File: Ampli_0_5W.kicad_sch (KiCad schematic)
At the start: 69 parts, among them J1002 RF_In, J1003 PTT_In, J1005 Aux_PTT_Out, J1006 RF_Out, Q1001 2N7002, Q1002 FDD6685, Q1005 2N5109, Q1006 AFT05MP075N, T1001 4:1, T1002 1:1, T1003 1:9, U1001 L78L05_SO8

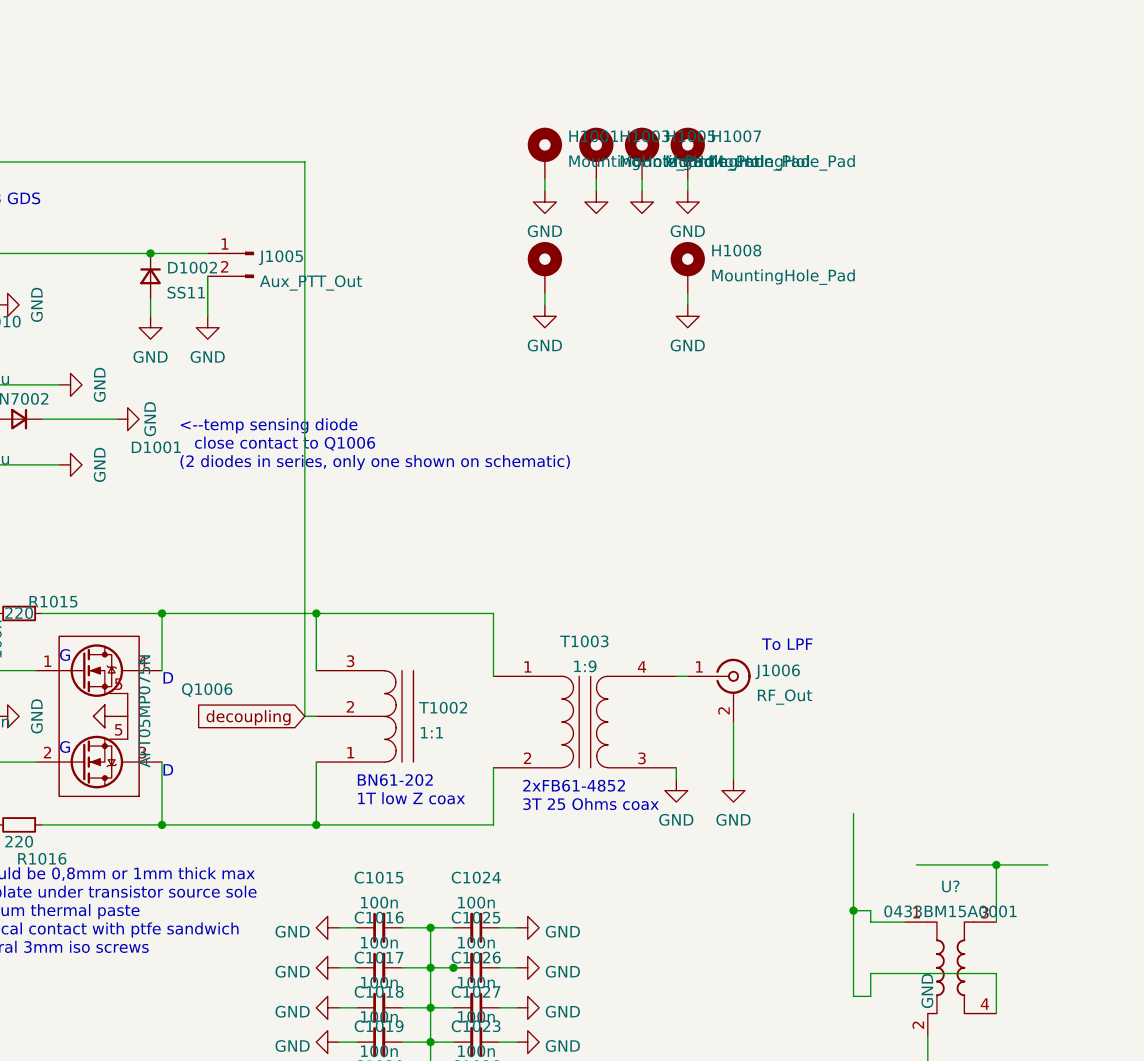
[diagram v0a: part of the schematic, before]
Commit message: release 2.0, shorter drain path
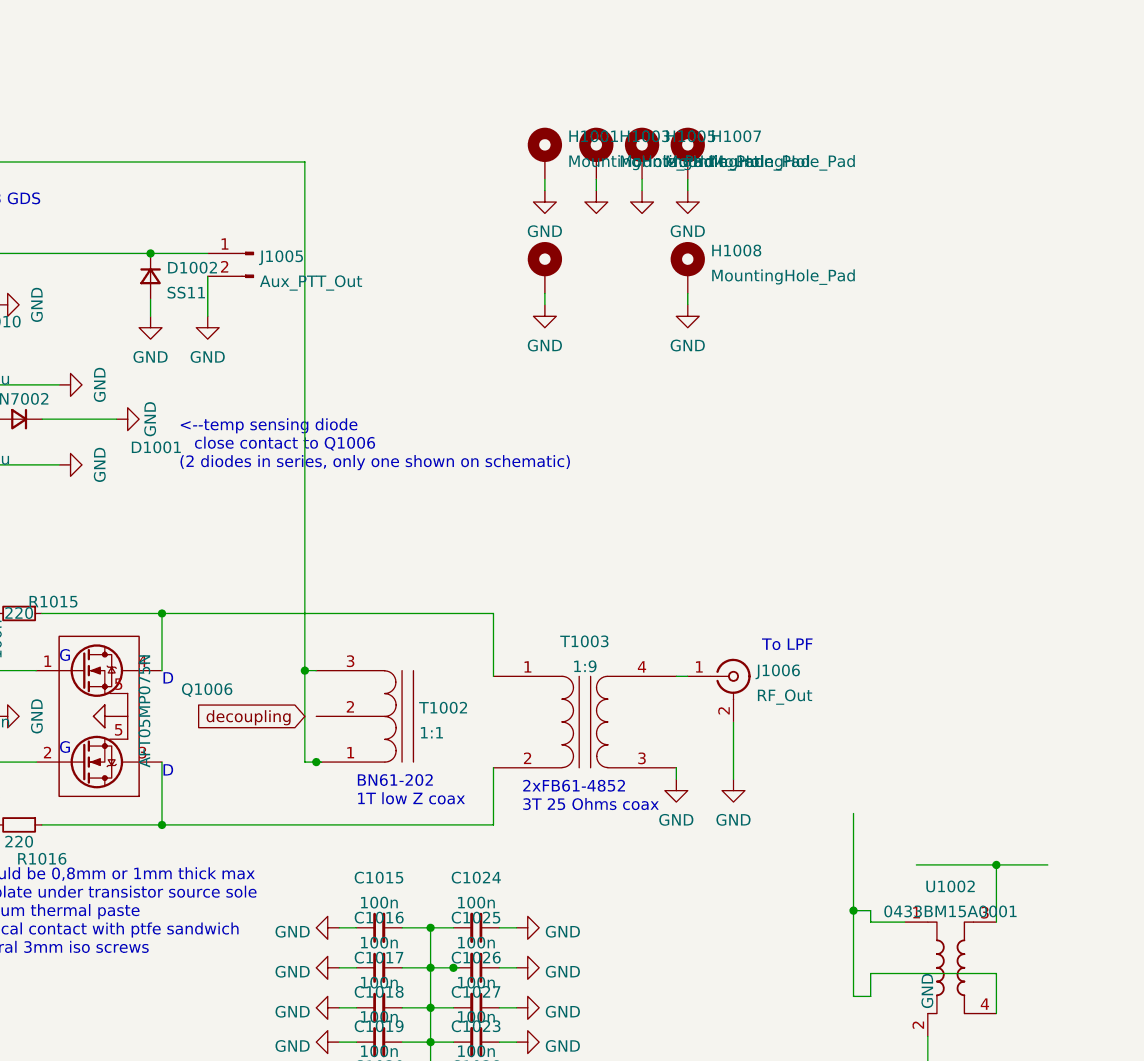
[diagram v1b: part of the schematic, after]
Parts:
- C1013, C1014: footprint Capacitor_SMD:C_0805_2012Metric_Pad1.18x1.45mm_HandSolder -> Capacitor_SMD:C_1206_3216Metric_Pad1.33x1.80mm_HandSolder
- C1015, C1016, C1017, C1018, C1019, C1020, C1021, C1022, C1023, C1024, C1025, C1026, C1027, C1028, C1029, C1030: footprint Capacitor_SMD:C_0805_2012Metric_Pad1.18x1.45mm_HandSolder -> Capacitor_SMD:C_1210_3225Metric_Pad1.33x2.70mm_HandSolder
- gave numbers to parts that had none: 1
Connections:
- net +12V: now also T1002.1 (SA), T1002.3 (SC); no longer T1002.2 (SB)
- net at Q1006.3 (D), R1016.1, T1003.2 (AB): no longer T1002.1 (SA)
- net at Q1006.4 (D), R1015.1, T1003.1 (AA): no longer T1002.3 (SC)

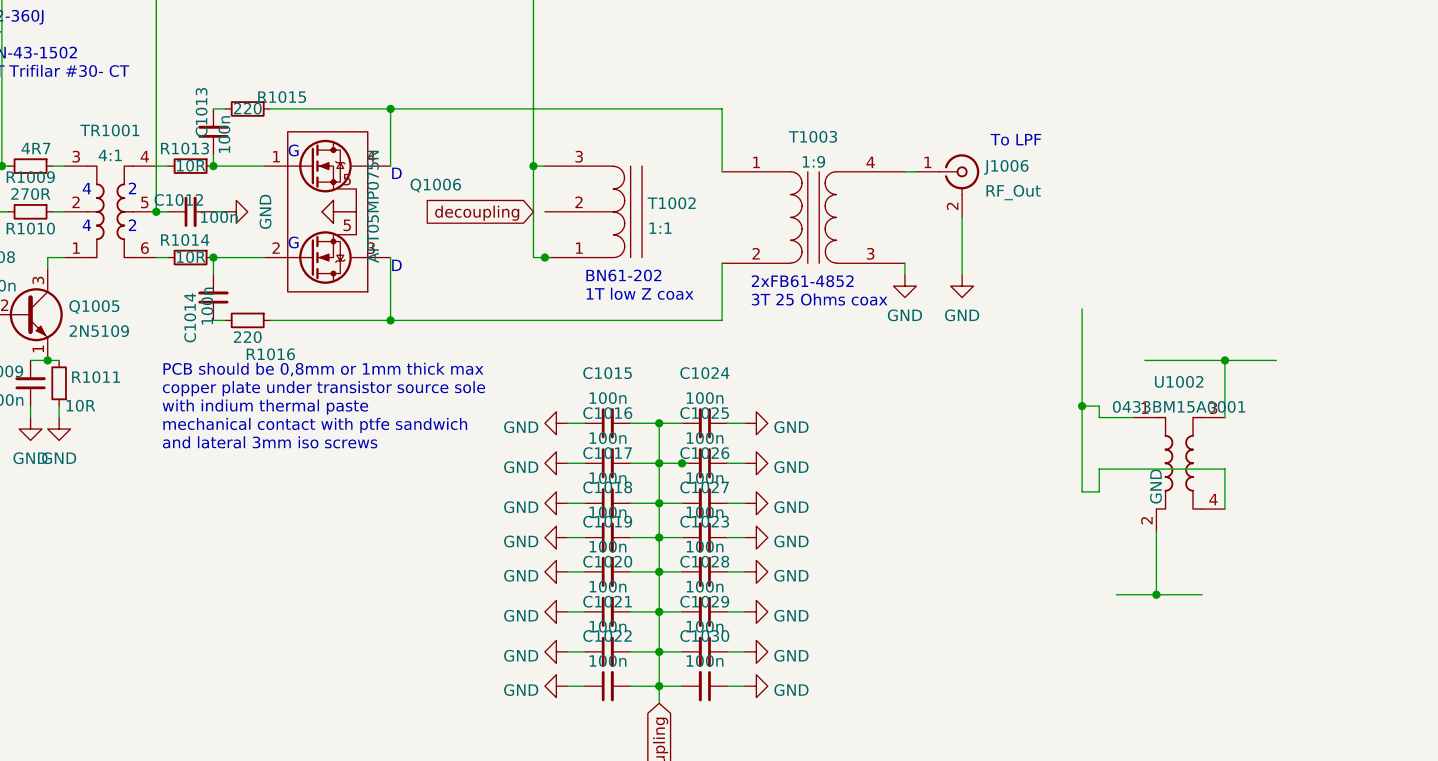
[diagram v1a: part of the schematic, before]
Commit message: shorten drain circuit, new gerber, new ibom
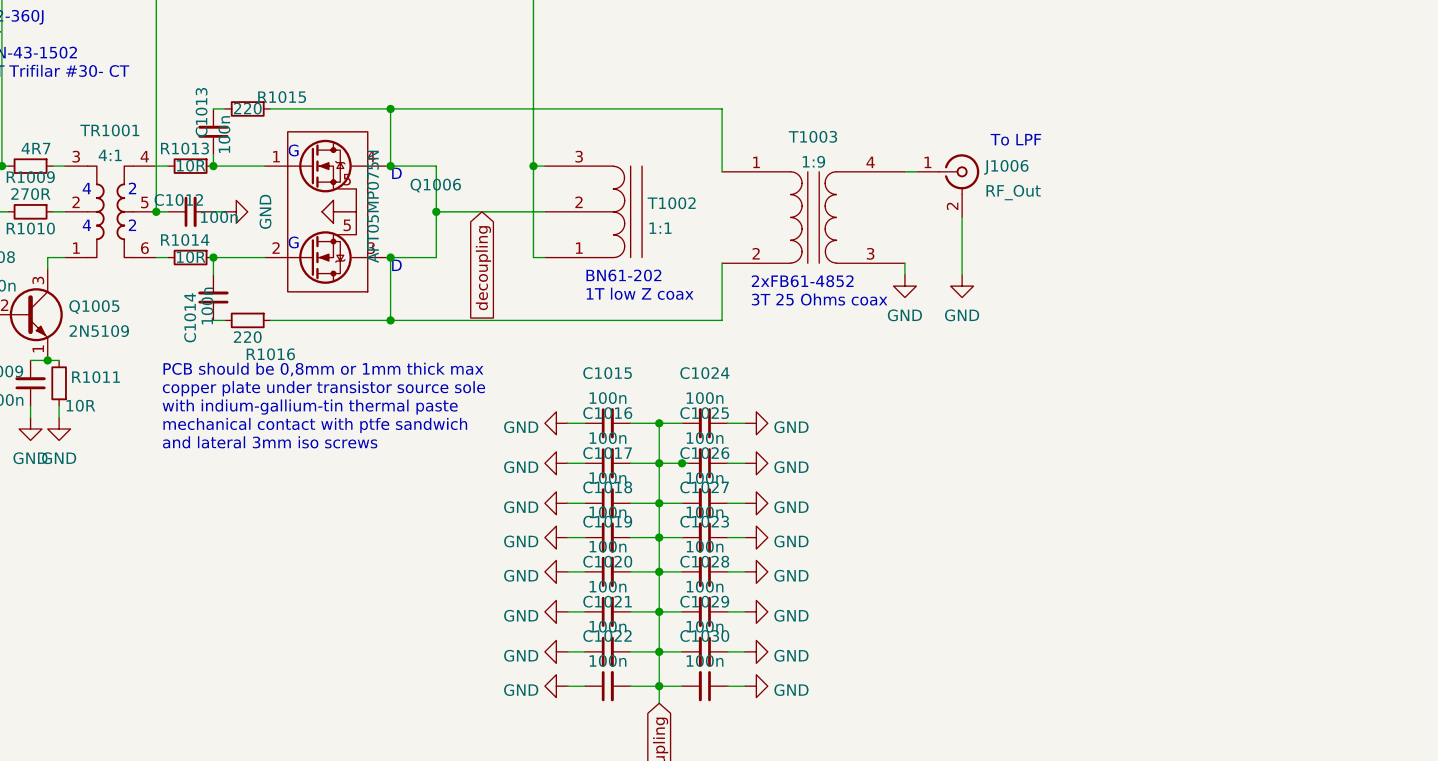
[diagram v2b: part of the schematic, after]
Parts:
- removed U1002: 0433BM15A0001, RF_Converter:Balun_Johanson_0896BM15A0001, symbol Transformer:0433BM15A0001
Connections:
- net +12V: no longer C1015.2, C1016.2, C1017.2, C1018.2, C1019.2, C1020.2, C1021.2, C1022.2, C1023.2, C1024.2, C1025.2, C1026.2, C1027.2, C1028.2, C1029.2, C1030.2
- net decoupling: now reaches Q1006.3 (D), R1016.1, T1003.2 (AB)
- net decoupling: now also C1015.2, C1016.2, C1017.2, C1018.2, C1019.2, C1020.2, C1021.2, C1022.2, C1023.2, C1024.2, C1025.2, C1026.2, C1027.2, C1028.2, C1029.2, C1030.2, Q1006.4 (D), R1015.1, T1002.2 (SB), T1003.1 (AA)
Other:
- note added: "PCB should be 0,8mm or 1mm thick max copper plate under transistor source sole with indium-gallium-tin thermal paste mechanical contact with ptfe sandwich and lateral 3mm iso screws"
- note removed: "PCB should be 0,8mm or 1mm thick max copper plate under transistor source sole with indium thermal paste mechanical contact with ptfe sandwich and lateral 3mm iso screws"
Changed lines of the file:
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@@
   (junction (at 146.05 151.13) (diameter 0) (color 0 0 0 0)
   )
-  (junction (at 201.295 140.97) (diameter 0) (color 0 0 0 0)
+  (junction (at 121.285 98.425) (diameter 0) (color 0 0 0 0)
   )
   (junction (at 43.815 36.83) (diameter 0) (color 0 0 0 0)
@@
   (junction (at 90.17 70.485) (diameter 0) (color 0 0 0 0)
   )
-  (junction (at 208.915 114.935) (diameter 0) (color 0 0 0 0)
-  )
   (junction (at 146.05 138.43) (diameter 0) (color 0 0 0 0)
   )
@@
   (junction (at 50.165 54.61) (diameter 0) (color 0 0 0 0)
   )
-  (junction (at 133.35 103.505) (diameter 0) (color 0 0 0 0)
-  )
   (junction (at 59.055 36.83) (diameter 0) (color 0 0 0 0)
   )
@@
   (junction (at 146.05 121.92) (diameter 0) (color 0 0 0 0)
   )
+  (junction (at 116.205 103.505) (diameter 0) (color 0 0 0 0)
+  )
   (junction (at 116.205 110.49) (diameter 0) (color 0 0 0 0)
   )
-  (junction (at 193.04 120.015) (diameter 0) (color 0 0 0 0)
-  )
   (junction (at 146.05 142.875) (diameter 0) (color 0 0 0 0)
   )
@@
   (junction (at 70.485 98.425) (diameter 0) (color 0 0 0 0)
   )
+  (junction (at 116.205 93.345) (diameter 0) (color 0 0 0 0)
+  )
   (junction (at 116.205 86.995) (diameter 0) (color 0 0 0 0)
   )
@@
     (stroke (width 0) (type default) (color 0 0 0 0))
   )
-  (wire (pts (xy 196.85 140.97) (xy 201.295 140.97))
-    (stroke (width 0) (type default) (color 0 0 0 0))
-  )
   (wire (pts (xy 116.205 103.505) (xy 116.205 110.49))
     (stroke (width 0) (type default) (color 0 0 0 0))
@@
     (stroke (width 0) (type default) (color 0 0 0 0))
   )
-  (wire (pts (xy 193.04 109.22) (xy 193.04 120.015))
-    (stroke (width 0) (type default) (color 0 0 0 0))
-  )
   (wire (pts (xy 132.08 93.345) (xy 133.35 93.345))
     (stroke (width 0) (type default) (color 0 0 0 0))
@@
     (stroke (width 0) (type default) (color 0 0 0 0))
   )
-  (wire (pts (xy 133.35 103.505) (xy 132.08 103.505))
-    (stroke (width 0) (type default) (color 0 0 0 0))
-  )
   (wire (pts (xy 142.875 130.81) (xy 146.05 130.81))
     (stroke (width 0) (type default) (color 0 0 0 0))
@@
     (stroke (width 0) (type default) (color 0 0 0 0))
   )
-  (wire (pts (xy 193.04 120.015) (xy 193.04 129.54))
-    (stroke (width 0) (type default) (color 0 0 0 0))
-  )
   (wire (pts (xy 63.5 41.91) (xy 65.405 41.91))
     (stroke (width 0) (type default) (color 0 0 0 0))
@@
     (stroke (width 0) (type default) (color 0 0 0 0))
   )
-  (wire (pts (xy 208.915 131.445) (xy 208.915 127))
-    (stroke (width 0) (type default) (color 0 0 0 0))
-  )
   (wire (pts (xy 65.405 108.585) (xy 65.405 109.855))
     (stroke (width 0) (type default) (color 0 0 0 0))
@@
     (stroke (width 0) (type default) (color 0 0 0 0))
   )
+  (wire (pts (xy 121.285 98.425) (xy 121.285 93.345))
+    (stroke (width 0) (type default) (color 0 0 0 0))
+  )
+  (wire (pts (xy 121.285 98.425) (xy 121.285 103.505))
+    (stroke (width 0) (type default) (color 0 0 0 0))
+  )
   (wire (pts (xy 96.52 98.425) (xy 97.79 98.425))
     (stroke (width 0) (type default) (color 0 0 0 0))
@@
     (stroke (width 0) (type default) (color 0 0 0 0))
   )
-  (wire (pts (xy 208.915 127) (xy 194.945 127))
-    (stroke (width 0) (type default) (color 0 0 0 0))
-  )
-  (wire (pts (xy 198.755 121.285) (xy 194.945 121.285))
-    (stroke (width 0) (type default) (color 0 0 0 0))
-  )
   (wire (pts (xy 50.165 54.61) (xy 51.435 54.61))
     (stroke (width 0) (type default) (color 0 0 0 0))
@@
     (stroke (width 0) (type default) (color 0 0 0 0))
   )
-  (wire (pts (xy 208.915 114.935) (xy 214.63 114.935))
-    (stroke (width 0) (type default) (color 0 0 0 0))
-  )
   (wire (pts (xy 146.05 142.875) (xy 146.05 138.43))
     (stroke (width 0) (type default) (color 0 0 0 0))
@@
     (stroke (width 0) (type default) (color 0 0 0 0))
   )
-  (wire (pts (xy 193.04 120.015) (xy 194.945 120.015))
-    (stroke (width 0) (type default) (color 0 0 0 0))
-  )
   (wire (pts (xy 78.105 114.935) (xy 79.375 114.935))
     (stroke (width 0) (type default) (color 0 0 0 0))
   )
+  (wire (pts (xy 132.08 103.505) (xy 133.35 103.505))
+    (stroke (width 0) (type default) (color 0 0 0 0))
+  )
   (wire (pts (xy 52.705 99.06) (xy 52.705 104.775))
     (stroke (width 0) (type default) (color 0 0 0 0))
@@
     (stroke (width 0) (type default) (color 0 0 0 0))
   )
-  (wire (pts (xy 201.295 140.97) (xy 206.375 140.97))
-    (stroke (width 0) (type default) (color 0 0 0 0))
-  )
-  (wire (pts (xy 200.025 114.935) (xy 208.915 114.935))
-    (stroke (width 0) (type default) (color 0 0 0 0))
-  )
   (wire (pts (xy 121.285 49.53) (xy 121.285 53.975))
     (stroke (width 0) (type default) (color 0 0 0 0))
@@
     (stroke (width 0) (type default) (color 0 0 0 0))
   )
-  (wire (pts (xy 208.915 121.285) (xy 208.915 114.935))
-    (stroke (width 0) (type default) (color 0 0 0 0))
-  )
   (wire (pts (xy 137.795 130.81) (xy 135.89 130.81))
     (stroke (width 0) (type default) (color 0 0 0 0))
@@
     (stroke (width 0) (type default) (color 0 0 0 0))
   )
-  (wire (pts (xy 194.945 127) (xy 194.945 129.54))
-    (stroke (width 0) (type default) (color 0 0 0 0))
-  )
   (wire (pts (xy 90.17 52.705) (xy 91.44 52.705))
     (stroke (width 0) (type default) (color 0 0 0 0))
@@
     (stroke (width 0) (type default) (color 0 0 0 0))
   )
-  (wire (pts (xy 201.295 133.985) (xy 201.295 140.97))
-    (stroke (width 0) (type default) (color 0 0 0 0))
-  )
   (wire (pts (xy 137.795 134.62) (xy 135.89 134.62))
     (stroke (width 0) (type default) (color 0 0 0 0))
@@
     (stroke (width 0) (type default) (color 0 0 0 0))
   )
-  (wire (pts (xy 194.945 120.015) (xy 194.945 121.285))
+  (wire (pts (xy 133.35 98.425) (xy 121.285 98.425))
     (stroke (width 0) (type default) (color 0 0 0 0))
   )
@@
     (stroke (width 0) (type default) (color 0 0 0 0))
   )
-  (wire (pts (xy 194.945 129.54) (xy 193.04 129.54))
+  (wire (pts (xy 121.285 103.505) (xy 116.205 103.505))
     (stroke (width 0) (type default) (color 0 0 0 0))
   )
@@
     (stroke (width 0) (type default) (color 0 0 0 0))
   )
+  (wire (pts (xy 116.205 93.345) (xy 121.285 93.345))
+    (stroke (width 0) (type default) (color 0 0 0 0))
+  )
   (wire (pts (xy 90.17 61.595) (xy 91.44 61.595))
     (stroke (width 0) (type default) (color 0 0 0 0))
@@
   )
   (wire (pts (xy 153.67 130.81) (xy 155.575 130.81))
-    (stroke (width 0) (type default) (color 0 0 0 0))
-  )
-  (wire (pts (xy 133.985 103.505) (xy 133.35 103.505))
     (stroke (width 0) (type default) (color 0 0 0 0))
   )
@@
     (effects (font (size 1.27 1.27)) (justify left bottom))
   )
-  (text "PCB should be 0,8mm or 1mm thick max\ncopper plate under transistor source sole \nwith indium thermal paste\nmechanical contact with ptfe sandwich\nand lateral 3mm iso screws"
+  (text "PCB should be 0,8mm or 1mm thick max\ncopper plate under transistor source sole \nwith indium-gallium-tin thermal paste\nmechanical contact with ptfe sandwich\nand lateral 3mm iso screws"
     (at 90.805 125.095 0)
     (effects (font (size 1.27 1.27)) (justify left bottom))
@@
     )
   )
-  (global_label "decoupling" (shape input) (at 132.08 98.425 180) (fields_autoplaced)
+  (global_label "decoupling" (shape input) (at 126.365 98.425 270) (fields_autoplaced)
     (effects (font (size 1.27 1.27)) (justify right))
-    (property "Intersheet References" "${INTERSHEET_REFS}" (id 0) (at 119.3255 98.3456 0)
+    (property "Intersheet References" "${INTERSHEET_REFS}" (id 0) (at 126.2856 111.1795 90)
       (effects (font (size 1.27 1.27)) (justify right) hide)
     )
@@
     (pin "2")
     (pin "3")
-  )
-  (symbol (lib_id "Transformer:0433BM15A0001") (at 203.835 126.365 0) (unit 1)
-    (in_bom yes) (on_board yes) (fields_autoplaced)
-    (property "Reference" "U1002" (id 0) (at 203.835 117.3693 0))
-    (property "Value" "0433BM15A0001" (id 1) (at 203.835 120.1444 0))
-    (property "Footprint" "RF_Converter:Balun_Johanson_0896BM15A0001" (id 2) (at 203.835 133.985 0)
-      (effects (font (size 1.27 1.27)) hide)
-    )
-    (property "Datasheet" "https://www.johansontechnology.com/datasheets/0433BM15A0001/0433BM15A0001.pdf" (id 3) (at 203.835 118.745 0)
-      (effects (font (size 1.27 1.27)) hide)
-    )
-    (pin "1")
-    (pin "2")
-    (pin "3")
-    (pin "4")
-    (pin "5")
-    (pin "6")
   )
   (symbol (lib_id "power:GND") (at 155.575 126.365 90) (unit 1)
@@
       (reference "U1001") (unit 1) (value "L78L05_SO8") (footprint "Package_SO:SOIC-8_3.9x4.9mm_P1.27mm")
     )
-    (path "/44d77947-e58b-4905-bc5c-c957fb08ea72"
-      (reference "U1002") (unit 1) (value "0433BM15A0001") (footprint "RF_Converter:Balun_Johanson_0896BM15A0001")
-    )
-  )
+  )

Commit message: Diomedes V1.0 final with correct psu, bias & drain trace
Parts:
- removed H1001, H1003: MountingHole_Pad, MountingHole:MountingHole_3.2mm_M3_DIN965_Pad, symbol Mechanical:MountingHole_Pad
- removed U1001: L78L05_SO8, Package_SO:SOIC-8_3.9x4.9mm_P1.27mm, symbol Regulator_Linear:L78L05_SO8
- added U1: LM78M05_TO252, Package_TO_SOT_SMD:TO-252-2, symbol Regulator_Linear:LM78M05_TO252
- renumbered C1003 to C1, C1001 to C10, C1012 to C11, C1013 to C12, C1014 to C13, C1015 to C14, C1016 to C15, C1017 to C16, C1018 to C17, C1019 to C18, C1020 to C19, C1004 to C2, C1021 to C20, C1022 to C21, C1024 to C22, C1025 to C23, C1026 to C24, C1027 to C25, C1023 to C26, C1028 to C27, C1029 to C28, C1030 to C29, C1005 to C3, C1006 to C4, C1007 to C5, C1008 to C6, C1009 to C7, C1010 to C8, C1011 to C9, D1001 to D1, D1002 to D2, H1006 to H1, H1004 to H2, H1002 to H4, H1005 to H6, H1007 to H7, H1008 to H8, J1002 to J1, J1003 to J2, J1005 to J3, J1006 to J4, Q1001 to Q1, Q1002 to Q2, Q1005 to Q3, Q1006 to Q4, R1002 to R1, R1011 to R10, R1012 to R11, R1013 to R12, R1014 to R13, R1015 to R14, R1016 to R15, R1003 to R2, R1004 to R3, R1005 to R4, R1006 to R5, R1007 to R6, R1008 to R7, R1009 to R8, R1010 to R9, RV1001 to RV1, T1001 to T1, T1002 to T2, T1003 to T3, TR1001 to TR1
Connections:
- net +12V: now also C14.2, C15.2, C16.2, C17.2, C18.2, C19.2, C20.2, C21.2, C22.2, C23.2, C24.2, C25.2, C26.2, C27.2, C28.2, C29.2, Q2.3 (S); no longer Q2.2 (D)
- net GND: now also U1.2 (GND)
- net at C8.1, RV1.1, RV1.2: now also U1.3 (VO)
- net at C5.1, D2.1 (K), J3.1 (Pin_1)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: now also Q2.2 (D), U1.1 (VI); no longer Q2.3 (S)
- removed net decoupling: C14.2, C15.2, C16.2, C17.2, C18.2, C19.2, C20.2, C21.2, C22.2, C23.2, C24.2, C25.2, C26.2, C27.2, C28.2, C29.2, Q4.3 (D), Q4.4 (D), R14.1, R15.1, T2.2 (SB), T3.1 (AA), T3.2 (AB)
- new net: Q4.3 (D), Q4.4 (D), R14.1, R15.1, T2.2 (SB), T3.1 (AA), T3.2 (AB)
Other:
- note added: "Ajouter une entrée tx to gnd (gate de Q1002)"
- note added: "From Red Pitaya - TX/RX E1-3 - Gnd E1 25/26 Active = high"
- note added: "Todo - Vérifier perçages de fixation - Vérifier contact semelle/pcb/gnd (plaquage transistor)"
- moved on the sheet: H6

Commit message: Diomedes V2.0 final, bias OK
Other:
- note added: "Todo - Vérifier perçages de fixation - Vérifier contact semelle/pcb/gnd"
- note removed: "Todo - Vérifier perçages de fixation - Vérifier contact semelle/pcb/gnd (plaquage transistor)"
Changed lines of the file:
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@@
     (effects (font (size 1.27 1.27)) (justify left bottom))
   )
-  (text "Todo\n- Vérifier perçages de fixation\n- Vérifier contact semelle/pcb/gnd (plaquage transistor) \n\n"
+  (text "Todo\n- Vérifier perçages de fixation\n- Vérifier contact semelle/pcb/gnd\n"
     (at 149.225 32.385 0)
     (effects (font (size 3 3)) (justify left bottom))

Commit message: new ibom, BEWARE, KICAD 7.0 FILE FORMAT
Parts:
- added J5, J6: RF_Out, SMA_PINS:SMA_PINS, symbol Connector:Conn_Coaxial
- added R16, R18: 62R, Resistor_SMD:R_0805_2012Metric_Pad1.20x1.40mm_HandSolder, symbol Device:R_Small
- added R17: 249R, Resistor_SMD:R_0805_2012Metric_Pad1.20x1.40mm_HandSolder, symbol Device:R_Small
- R5: value 6.8R -> 8.2R
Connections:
- net GND: now also J5.2 (Ext), J6.2 (Ext), R16.2, R18.2
- new net: J5.1 (In), R16.1, R17.2
- new net: J6.1 (In), R17.1, R18.1
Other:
- note added: "20dB"
- note added: "N.B. FR4, 0,8mm, Er 4.3, Cu 0.035mm strip 50 Ohms à 1.5mm"

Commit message: Kicad 7, new iBom, new temp diode cabling
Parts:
- removed J5, J6: RF_Out, SMA_PINS:SMA_PINS, symbol Connector:Conn_Coaxial
- removed R16, R18: 62R, Resistor_SMD:R_0805_2012Metric_Pad1.20x1.40mm_HandSolder, symbol Device:R_Small
- removed R17: 249R, Resistor_SMD:R_0805_2012Metric_Pad1.20x1.40mm_HandSolder, symbol Device:R_Small
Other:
- note added: "<--temp sensing diode close contact to Q1006 2 diodes in series, only one shown on schematic An and Ka solder pads on pcb (anode/cathode)"
- note removed: "20dB"
- note removed: "<--temp sensing diode close contact to Q1006 (2 diodes in series, only one shown on schematic)"
